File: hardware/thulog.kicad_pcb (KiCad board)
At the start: 2 copper layers, 37.8 x 30.7 mm, 17 parts, among them IC1 ATTINY2313A-S, K1 DHT, P1 ISP, P2 CONN_2, P3 CONN_2, X1 QUARTZCMS4

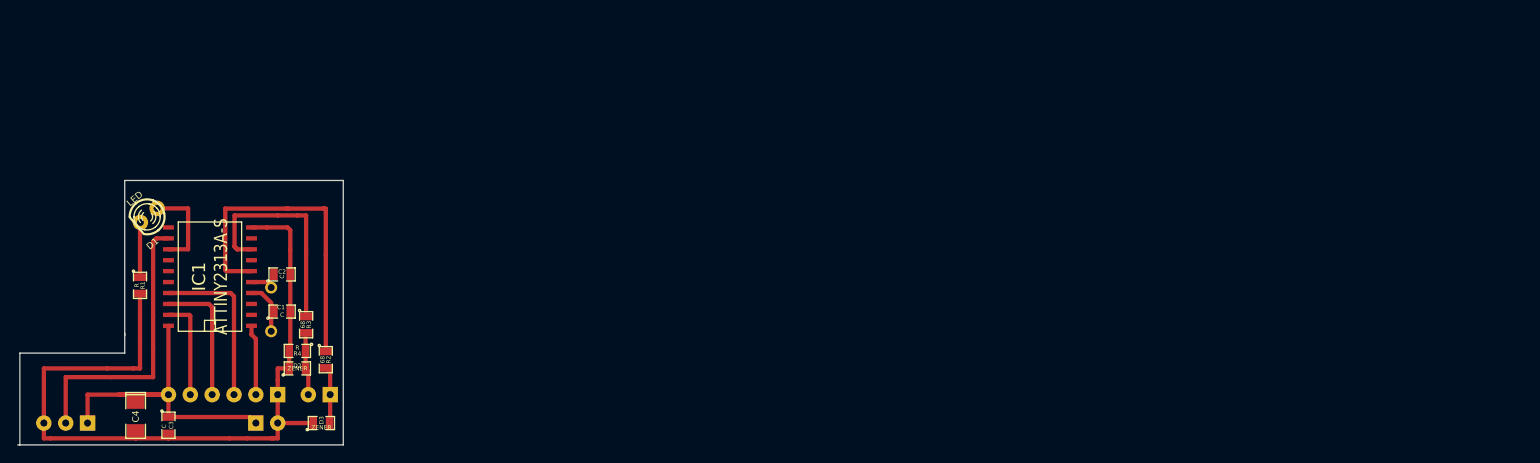
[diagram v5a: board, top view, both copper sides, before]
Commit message: finished with pbc, printed
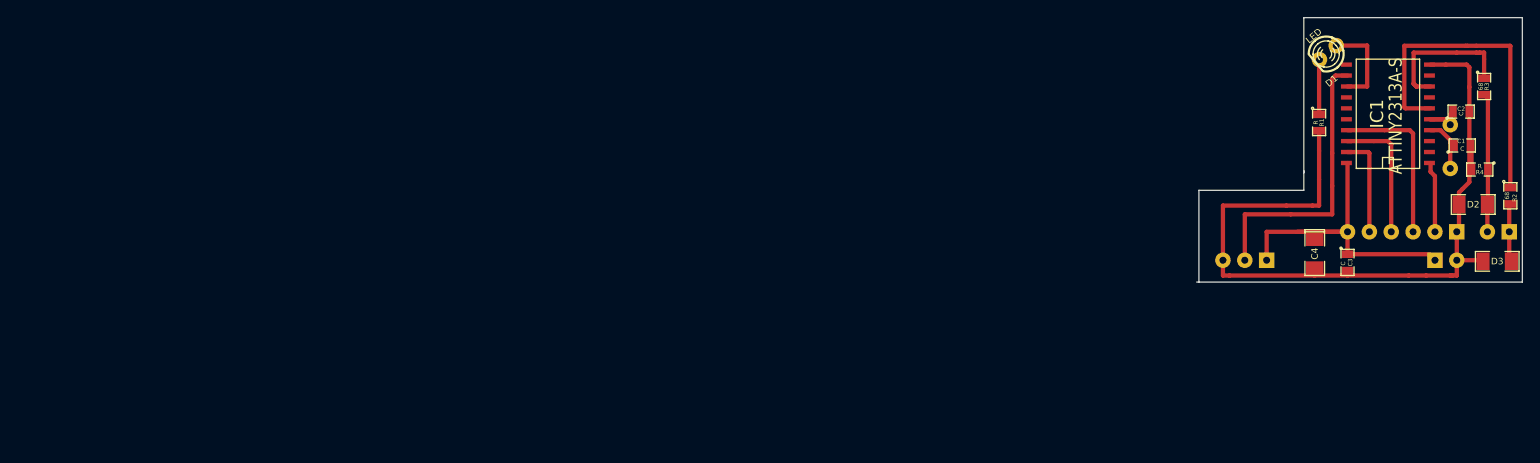
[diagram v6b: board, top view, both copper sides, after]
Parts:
- D2, D3: footprint SM0805 -> SM1206
- moved R3 139.7 mm to (273.8, 24.9)
- moved R4 139.0 mm to (273.3, 34.5)
- moved R2 139.0 mm to (276.9, 37.6)
- moved C1 138.5 mm to (271.3, 31.8)
- moved C3 138.3 mm to (257.9, 45.3)
- moved C4 138.3 mm to (254.1, 44.3)
- moved D1 138.3 mm to (255.7, 21.0)
- moved K1 138.3 mm to (246.0, 45.1)
- moved P2 138.3 mm to (275.5, 41.8)
- moved P3 138.3 mm to (269.4, 45.1)
- moved C2 138.3 mm to (271.1, 27.8)
- moved R1 138.3 mm to (254.6, 29.1)
- moved X1 138.3 mm to (269.9, 31.9)
- moved P1 138.3 mm to (264.3, 41.8)
- moved IC1 138.2 mm to (262.6, 28.1)
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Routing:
- net N-000008: track 26.2 -> 17.3 mm
- net N-0000023: track 7.33 -> 16.1 mm
- net N-0000014: track 2.15 -> 6.48 mm
- net GND: track 90.7 -> 91.7 mm
- net N-0000017: track 38.5 -> 39.0 mm

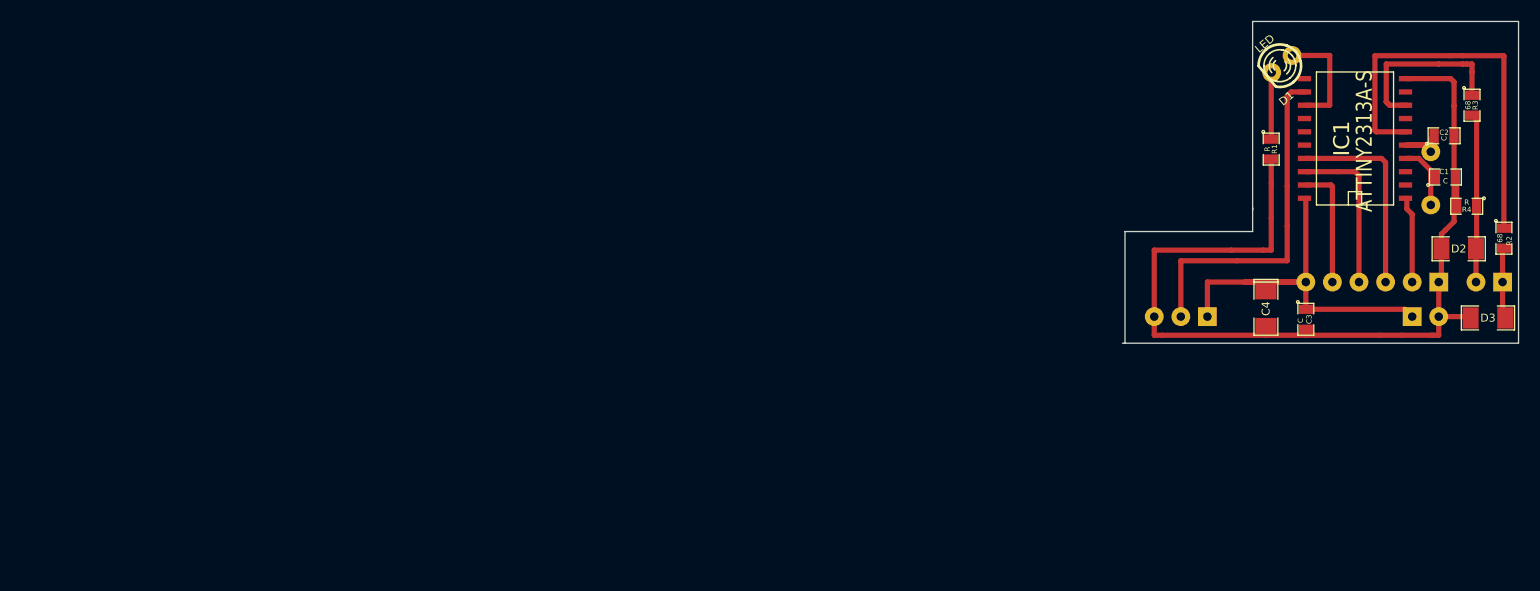
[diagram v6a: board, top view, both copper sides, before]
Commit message: fixed the d+ to VCC instead of GND, added usb mini-b instead of simple connection pads, minimized the pcb
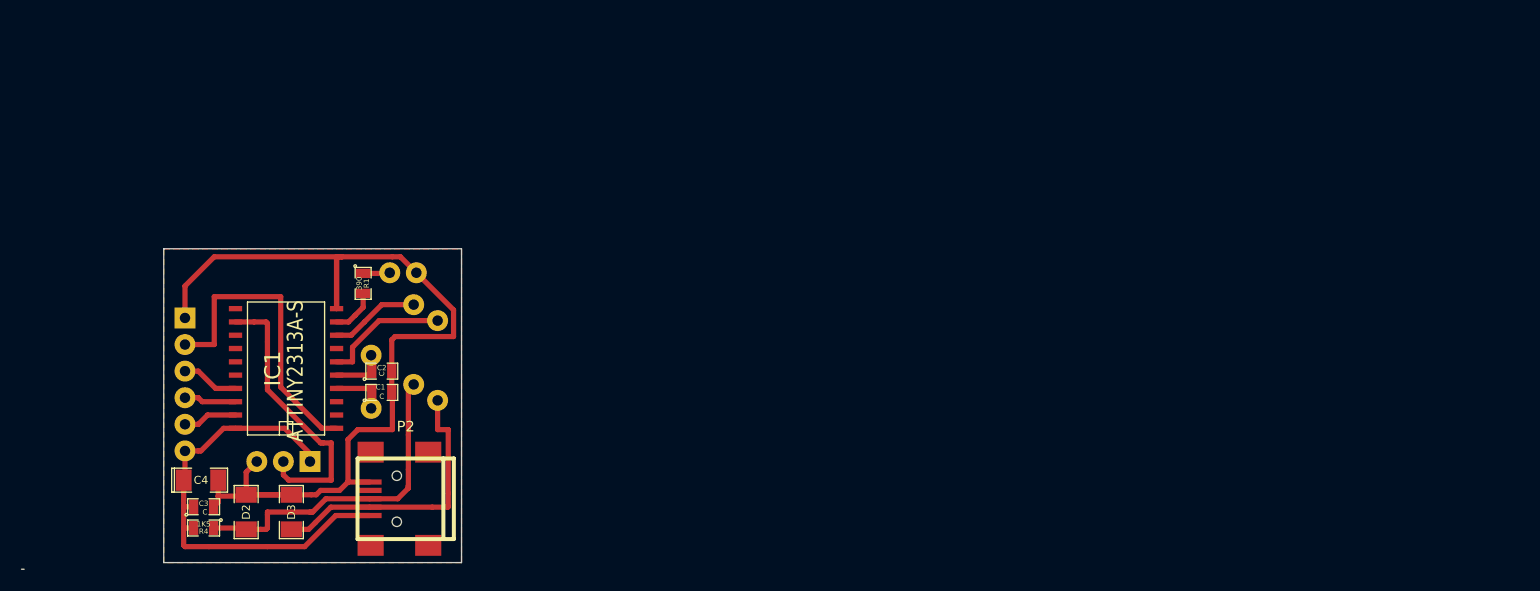
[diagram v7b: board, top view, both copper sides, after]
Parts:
- removed P3: CONN_2, SIL-2
- D1: moved to B.Cu
- P2: value CONN_2 -> USBmini; footprint SIL-2 -> USB_MINI_B; moved to F.Cu
- R1: value R -> 390
- R2, R3: footprint SM0805 -> R3; moved to B.Cu
- R4: value R -> 1K5
- moved R4 124.5 mm to (152.7, 65.3)
- moved D2 118.5 mm to (156.7, 63.8), turned to 270 degrees
- moved D3 115.8 mm to (161.0, 63.8), turned to 270 degrees
- moved P1 113.8 mm to (150.9, 51.6), turned to 270 degrees
- moved C3 106.8 mm to (152.7, 63.2), turned to 0 degrees
- moved P2 105.6 mm to (172.0, 62.5)
- moved IC1 104.4 mm to (160.5, 50.0)
- moved C2 103.9 mm to (169.7, 50.3)
- moved C1 103.7 mm to (169.7, 52.3)
- moved R3 103.6 mm to (172.7, 47.8)
- moved X1 103.1 mm to (168.7, 51.3)
- moved C4 103.0 mm to (152.4, 60.7), turned to 0 degrees
- moved R2 102.5 mm to (175.0, 49.3)
- moved R1 87.7 mm to (167.9, 41.9)
- moved K1 86.8 mm to (160.3, 58.9)
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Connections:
- D1 pad 2: N-000007 (its old number) -> GND
- D2 pad 2: N-0000023 (its old number) -> N-0000024
- D3 pad 2: N-0000022 -> N-0000025
- IC1 pad 13: N-0000010 -> (no net)
- IC1 pad 9: (no net) -> N-000009
- P2 pad 1: N-0000022 -> VCC
- P2 pad 2: N-0000023 (its old number) -> N-0000025
- R1 pad 1: N-000007 (its old number) -> N-0000010
- R1 pad 2: GND -> N-000009
- R2 pad 2: N-0000022 -> N-0000025
- R3 pad 2: N-0000023 (its old number) -> N-0000024
- R4 pad 1: N-0000023 (its old number) -> N-0000024
- R4 pad 2: GND -> VCC
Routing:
- net N-0000024: track 0.00 -> 31.8 mm
- net N-0000025: track 0.00 -> 27.6 mm
- net N-0000017: track 39.0 -> 12.1 mm
- net RESET: track 8.08 -> 29.3 mm
- net N-0000023 (its old number): track 16.1 -> 0.00 mm
- net N-000003: track 19.2 -> 5.51 mm
- net N-000005: track 15.4 -> 4.98 mm
- net N-0000013: track 17.3 -> 8.58 mm
- net N-0000010: track 10.6 -> 2.57 mm
- net N-0000022: track 6.62 -> 0.00 mm
- net N-000004: track 11.7 -> 5.19 mm
- net N-000007 (its old number): track 6.38 -> 0.00 mm
- net N-000007: track 33.2 -> 27.3 mm
- net N-000009: track 0.00 -> 4.45 mm
- net VCC: track 40.7 -> 44.6 mm
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- added copper zone on F.Cu, net (none)
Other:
- board size 37.8 x 30.7 mm -> 42 x 30.6 mm

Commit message: small changes in pcb
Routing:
- net VCC: track 44.6 -> 48.5 mm
- net GND: track 93.6 -> 95.9 mm
- net N-000007: track 27.3 -> 28.8 mm
- net N-0000025: track 27.6 -> 28.7 mm
- net RESET: track 29.3 -> 30.4 mm
- net N-000003: track 5.51 -> 6.40 mm
- net N-0000024: track 31.8 -> 32.5 mm
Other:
- board size 42 x 30.6 mm -> 28.4 x 30 mm
